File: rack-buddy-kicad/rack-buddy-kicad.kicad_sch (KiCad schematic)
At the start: 15 parts, among them J1 GPIO, U1 CAT24C256

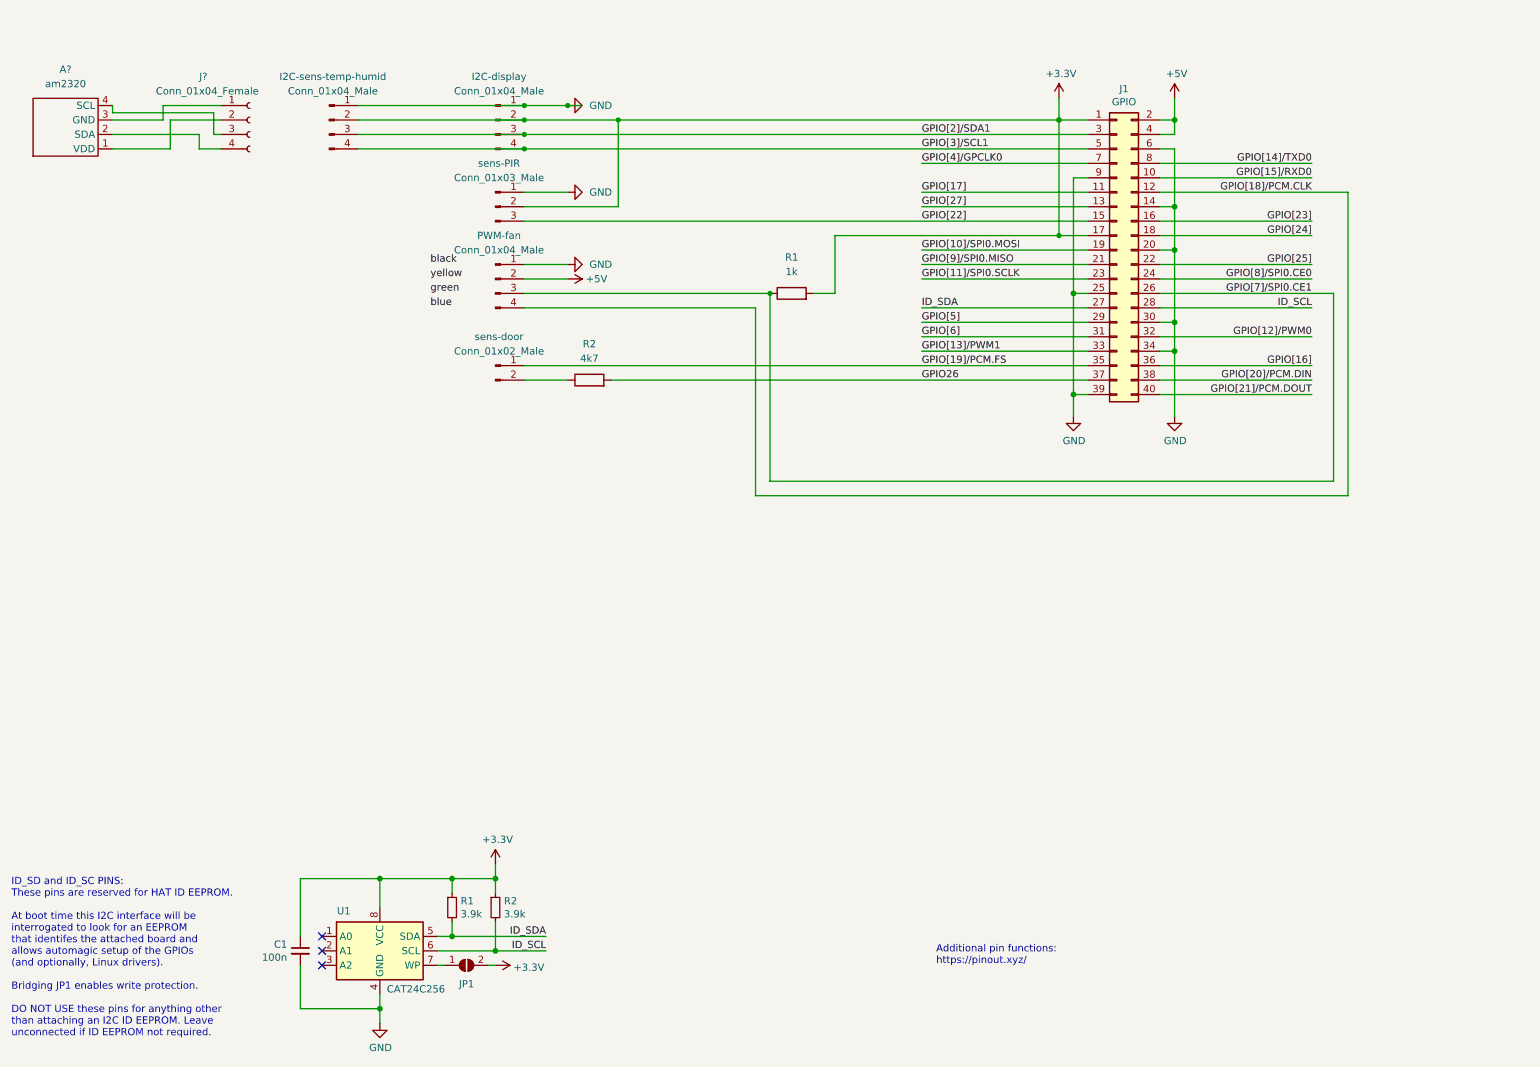
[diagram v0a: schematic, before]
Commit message: Update rack-buddy schematics/wiring
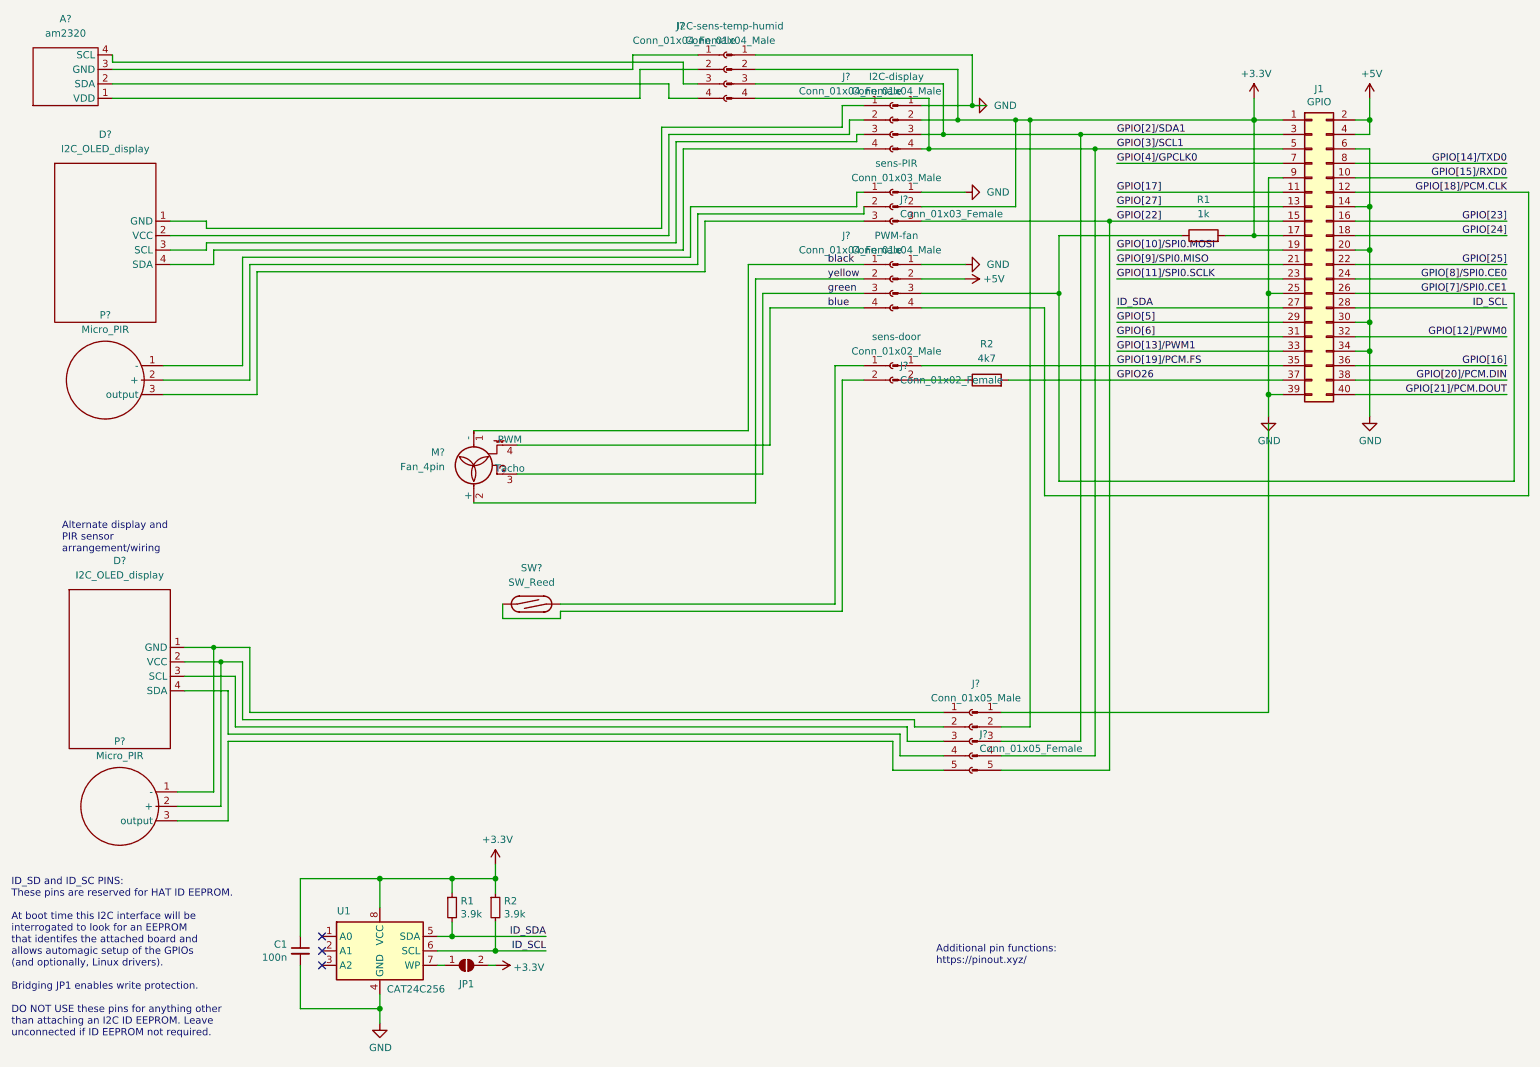
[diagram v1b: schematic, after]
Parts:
- added D? (x2): I2C_OLED_display, symbol Display_Graphic:I2C_OLED_display
- added J? (x2): Conn_01x04_Female, Connector_JST:JST_XH_B4B-XH-A_1x04_P2.50mm_Vertical, symbol Connector:Conn_01x04_Female
- added J?: Conn_01x05_Male, symbol Connector:Conn_01x05_Male
- added J?: Conn_01x02_Female, symbol Connector:Conn_01x02_Female
- added J?: Conn_01x03_Female, symbol Connector:Conn_01x03_Female
- added J?: Conn_01x05_Female, symbol Connector:Conn_01x05_Female
- added M?: Fan_4pin, symbol Motor:Fan_4pin
- added P? (x2): Micro_PIR, symbol Sensor_Optical:Micro_PIR
- added SW?: SW_Reed, symbol Switch:SW_Reed
- I2C-display, J?: footprint (none) -> Connector_JST:JST_XH_B4B-XH-A_1x04_P2.50mm_Vertical
- sens-PIR: footprint (none) -> Connector_JST:JST_XH_B3B-XH-A_1x03_P2.50mm_Vertical
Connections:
- net +3V3: now also J?.2 (Pin_2)
- net GPIO[22]: now also J?.5 (Pin_5)
- net GPIO[2]/SDA1: now also J?.3 (Pin_3)
- net GPIO[3]/SCL1: now also J?.4 (Pin_4)
- net black: now also J?.1 (Pin_1), M?.1 (-)
- net blue: now also J?.4 (Pin_4), M?.4 (PWM)
- net green: now also J?.3 (Pin_3), M?.3 (Tacho)
- net yellow: now also J?.2 (Pin_2), M?.2 (+)
- new net: D?.1 (GND), J?.1 (Pin_1)
- new net: D?.2 (VCC), J?.2 (Pin_2)
- new net: D?.3 (SCL), J?.3 (Pin_3) (x2)
- new net: D?.4 (SDA), J?.4 (Pin_4) (x2)
- new net: D?.1 (GND), J?.1 (Pin_1), P?.1 (-)
- new net: D?.2 (VCC), J?.2 (Pin_2), P?.2 (+)
- new net: J?.2 (Pin_2), SW?.1
- new net: J?.1 (Pin_1), SW?.2
- new net: J?.5 (Pin_5), P?.3 (output)
- new net: J?.1 (Pin_1), P?.1 (-)
- new net: J?.2 (Pin_2), P?.2 (+)
- new net: J?.3 (Pin_3), P?.3 (output)
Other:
- note added: "Alternate display and PIR sensor arrangement/wiring"
- moved on the sheet: A?, I2C-display, I2C-sens-temp-humid, J1, J?, PWM-fan, R1, R2, sens-PIR, sens-door
